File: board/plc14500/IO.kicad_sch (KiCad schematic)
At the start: 72 parts, among them U1 74HC14, U2 4051, U3 74HC14, U5 4099

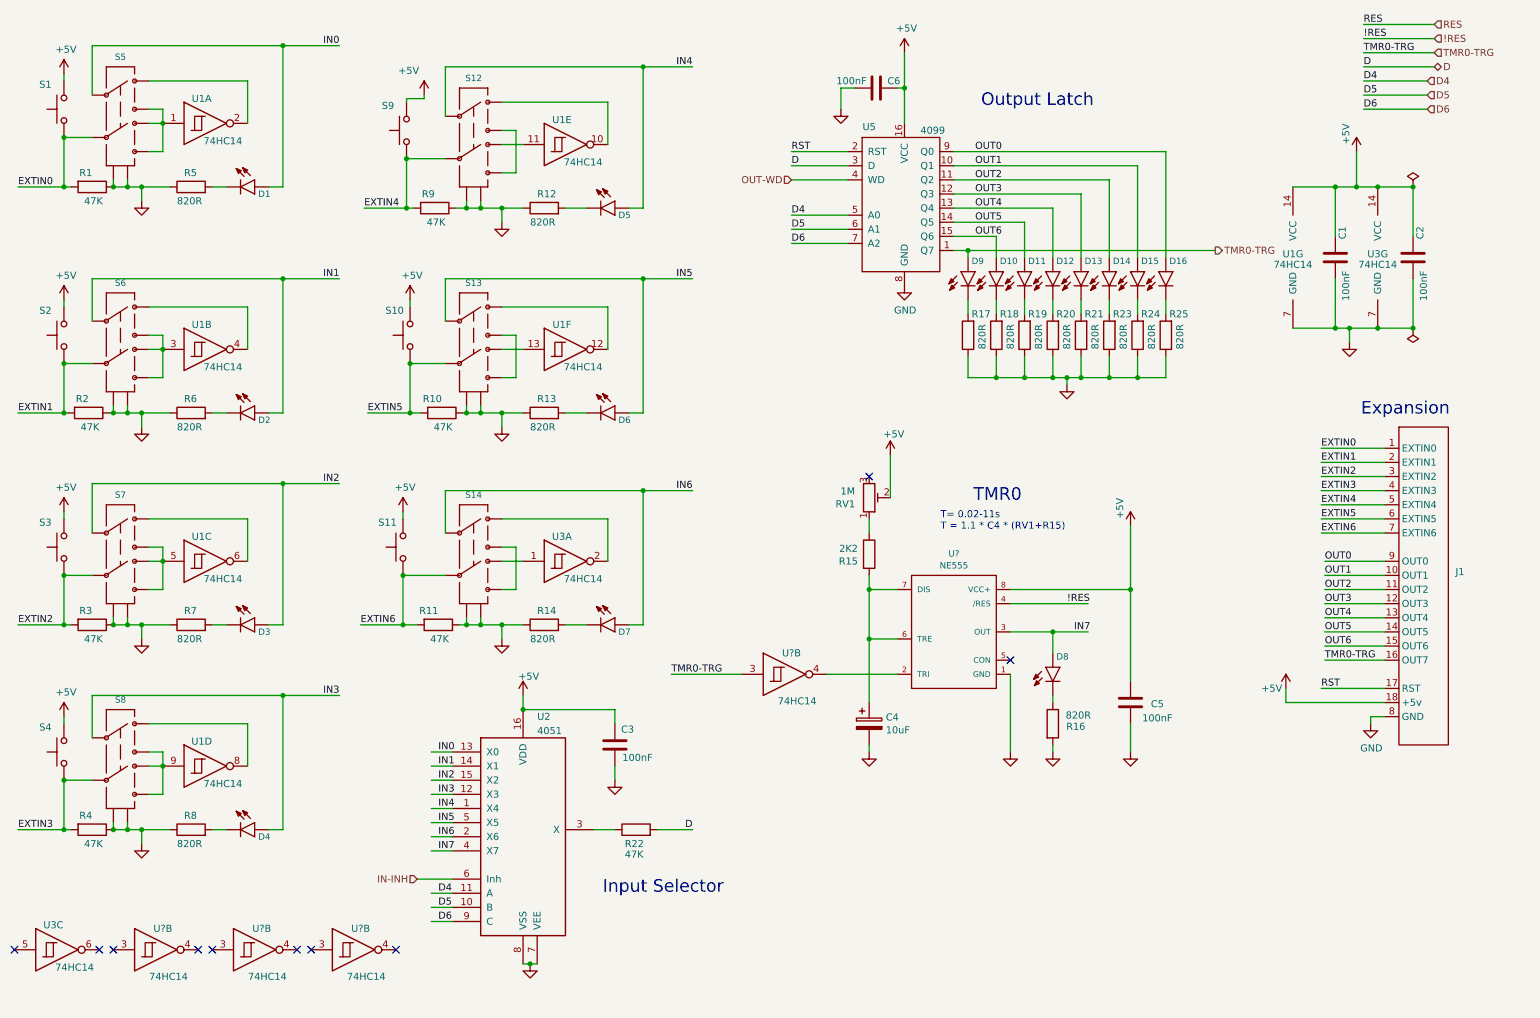
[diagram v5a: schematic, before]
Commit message: Fix issues on REV.D0
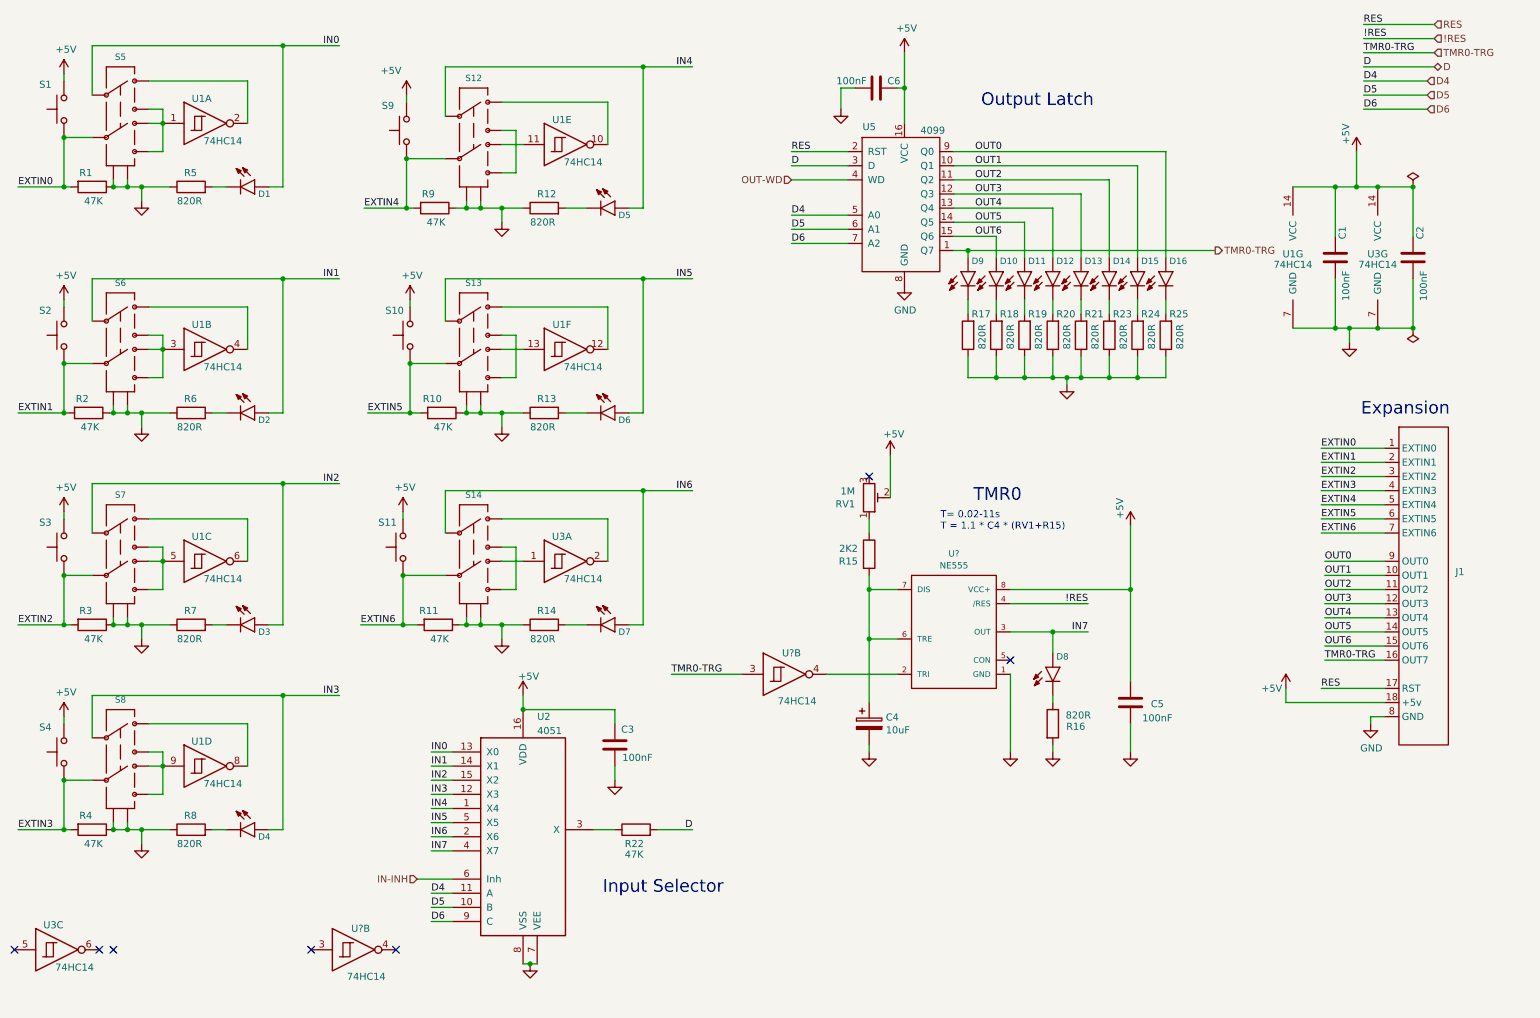
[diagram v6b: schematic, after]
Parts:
- removed U? (x2): 74HC14, Package_DIP:DIP-14_W7.62mm_LongPads, symbol plc14500:74HC14
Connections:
- net RST is gone; now on net RES: J1.17 (RST), U5.2 (RST)
- no-connect marks 10 -> 7
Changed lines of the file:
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@@
   (junction (at 105.41 142.24) (diameter 0) (color 0 0 0 0)
   )
-  (no_connect (at 46.99 185.42))
   (no_connect (at 29.21 185.42))
-  (no_connect (at 64.77 185.42))
-  (no_connect (at 49.53 185.42))
   (no_connect (at 67.31 185.42))
   (no_connect (at 167.64 100.33))
@@
     (stroke (width 0) (type default))
   )
-  (wire (pts (xy 84.455 32.385) (xy 84.455 33.02))
+  (wire (pts (xy 84.455 31.75) (xy 84.455 33.02))
     (stroke (width 0) (type default))
   )
@@
     (stroke (width 0) (type default))
   )
-  (wire (pts (xy 87.63 32.385) (xy 87.63 31.75))
-    (stroke (width 0) (type default))
-  )
   (wire (pts (xy 36.83 91.44) (xy 36.83 88.9))
     (stroke (width 0) (type default))
@@
     (stroke (width 0) (type default))
   )
-  (wire (pts (xy 84.455 32.385) (xy 87.63 32.385))
-    (stroke (width 0) (type default))
-  )
   (wire (pts (xy 172.72 30.48) (xy 173.99 30.48))
     (stroke (width 0) (type default))
@@
     (effects (font (size 2.2606 2.2606)) (justify right bottom))
   )
-  (label "IN0" (at 90.17 149.86 0) (fields_autoplaced)
+  (label "IN0" (at 88.9 149.86 0) (fields_autoplaced)
     (effects (font (size 1.27 1.27)) (justify left bottom))
   )
@@
     (effects (font (size 1.27 1.27)) (justify left bottom))
   )
-  (label "IN2" (at 90.17 154.94 0) (fields_autoplaced)
+  (label "IN2" (at 88.9 154.94 0) (fields_autoplaced)
     (effects (font (size 1.27 1.27)) (justify left bottom))
   )
@@
     (effects (font (size 1.27 1.27)) (justify left bottom))
   )
-  (label "D4" (at 90.17 175.26 0) (fields_autoplaced)
+  (label "D4" (at 88.9 175.26 0) (fields_autoplaced)
     (effects (font (size 1.27 1.27)) (justify left bottom))
   )
-  (label "RST" (at 153.67 41.91 0) (fields_autoplaced)
+  (label "RES" (at 153.67 41.91 0) (fields_autoplaced)
     (effects (font (size 1.27 1.27)) (justify left bottom))
   )
@@
     (effects (font (size 1.27 1.27)) (justify right bottom))
   )
-  (label "IN7" (at 204.47 128.27 0) (fields_autoplaced)
-    (effects (font (size 1.27 1.27)) (justify left bottom))
+  (label "IN7" (at 207.01 128.27 180) (fields_autoplaced)
+    (effects (font (size 1.27 1.27)) (justify right bottom))
   )
   (label "D4" (at 153.67 53.34 0) (fields_autoplaced)
@@
     (effects (font (size 1.27 1.27)) (justify right bottom))
   )
-  (label "!RES" (at 203.2 123.19 0) (fields_autoplaced)
-    (effects (font (size 1.27 1.27)) (justify left bottom))
+  (label "!RES" (at 207.01 123.19 180) (fields_autoplaced)
+    (effects (font (size 1.27 1.27)) (justify right bottom))
   )
-  (label "IN1" (at 90.17 152.4 0) (fields_autoplaced)
+  (label "IN1" (at 88.9 152.4 0) (fields_autoplaced)
     (effects (font (size 1.27 1.27)) (justify left bottom))
   )
@@
     (effects (font (size 1.27 1.27)) (justify left bottom))
   )
-  (label "IN5" (at 90.17 162.56 0) (fields_autoplaced)
+  (label "IN5" (at 88.9 162.56 0) (fields_autoplaced)
     (effects (font (size 1.27 1.27)) (justify left bottom))
   )
@@
     (effects (font (size 1.27 1.27)) (justify left bottom))
   )
-  (label "D6" (at 90.17 180.34 0) (fields_autoplaced)
+  (label "D6" (at 88.9 180.34 0) (fields_autoplaced)
     (effects (font (size 1.27 1.27)) (justify left bottom))
   )
@@
     (effects (font (size 1.27 1.27)) (justify left bottom))
   )
-  (label "IN7" (at 90.17 167.64 0) (fields_autoplaced)
+  (label "IN7" (at 88.9 167.64 0) (fields_autoplaced)
     (effects (font (size 1.27 1.27)) (justify left bottom))
   )
@@
     (effects (font (size 1.27 1.27)) (justify left bottom))
   )
-  (label "RST" (at 248.92 138.43 0) (fields_autoplaced)
+  (label "RES" (at 248.92 138.43 0) (fields_autoplaced)
     (effects (font (size 1.27 1.27)) (justify left bottom))
   )
@@
     (effects (font (size 1.27 1.27)) (justify left bottom))
   )
-  (label "IN4" (at 90.17 160.02 0) (fields_autoplaced)
+  (label "IN4" (at 88.9 160.02 0) (fields_autoplaced)
     (effects (font (size 1.27 1.27)) (justify left bottom))
   )
@@
     (effects (font (size 1.27 1.27)) (justify right bottom))
   )
-  (label "D5" (at 90.17 177.8 0) (fields_autoplaced)
+  (label "D5" (at 88.9 177.8 0) (fields_autoplaced)
     (effects (font (size 1.27 1.27)) (justify left bottom))
   )
@@
     (effects (font (size 1.27 1.27)) (justify left bottom))
   )
-  (label "IN6" (at 90.17 165.1 0) (fields_autoplaced)
+  (label "IN6" (at 88.9 165.1 0) (fields_autoplaced)
     (effects (font (size 1.27 1.27)) (justify left bottom))
   )
@@
     (effects (font (size 1.27 1.27)) (justify left bottom))
   )
-  (label "IN3" (at 90.17 157.48 0) (fields_autoplaced)
+  (label "IN3" (at 88.9 157.48 0) (fields_autoplaced)
     (effects (font (size 1.27 1.27)) (justify left bottom))
   )
@@
     )
   )
-  (symbol (lib_id "power:+5V") (at 87.63 31.75 0) (unit 1)
+  (symbol (lib_id "power:+5V") (at 84.455 31.75 0) (unit 1)
     (in_bom yes) (on_board yes) (dnp no)
-    (property "Reference" "#PWR015" (at 87.63 35.56 0)
+    (property "Reference" "#PWR015" (at 84.455 35.56 0)
       (effects (font (size 1.27 1.27)) hide)
     )
-    (property "Value" "+5V" (at 84.836 27.3558 0)
+    (property "Value" "+5V" (at 81.661 27.3558 0)
       (effects (font (size 1.27 1.27)))
     )
-    (property "Footprint" "" (at 87.63 31.75 0)
+    (property "Footprint" "" (at 84.455 31.75 0)
       (effects (font (size 1.27 1.27)) hide)
     )
-    (property "Datasheet" "" (at 87.63 31.75 0)
+    (property "Datasheet" "" (at 84.455 31.75 0)
       (effects (font (size 1.27 1.27)) hide)
     )
@@
     )
   )
-  (symbol (lib_id "plc14500:74HC14") (at 39.37 185.42 0) (unit 2)
-    (in_bom yes) (on_board yes) (dnp no)
-    (property "Reference" "U?" (at 40.64 181.61 0)
-      (effects (font (size 1.27 1.27)))
-    )
-    (property "Value" "74HC14" (at 41.656 190.246 0)
-      (effects (font (size 1.27 1.27)))
-    )
-    (property "Footprint" "Package_DIP:DIP-14_W7.62mm_LongPads" (at 39.37 185.42 0)
-      (effects (font (size 1.27 1.27)) hide)
-    )
-    (property "Datasheet" "http://www.ti.com/lit/gpn/sn74HC14" (at 39.37 185.42 0)
-      (effects (font (size 1.27 1.27)) hide)
-    )
-    (property "Price" "0.16" (at 39.37 185.42 0)
-      (effects (font (size 1.27 1.27)) hide)
-    )
-    (pin "1")
-    (pin "2")
-    (pin "3")
-    (pin "4")
-    (pin "5")
-    (pin "6")
-    (pin "8")
-    (pin "9")
-    (pin "10")
-    (pin "11")
-    (pin "12")
-    (pin "13")
-    (pin "14")
-    (pin "7")
-    (instances
-      (project "plc14500"
-        (path "/e5c24396-229a-4727-a88d-8f28d7f70179/00000000-0000-0000-0000-00006394a5b3"
-          (reference "U?") (unit 2)
-        )
-        (path "/e5c24396-229a-4727-a88d-8f28d7f70179"
-          (reference "U?") (unit 1)
-        )
-        (path "/e5c24396-229a-4727-a88d-8f28d7f70179/00000000-0000-0000-0000-000063b4bda9"
-          (reference "U11") (unit 4)
-        )
-      )
-    )
-  )
   (symbol (lib_id "Device:C") (at 251.46 60.96 180) (unit 1)
     (in_bom yes) (on_board yes) (dnp no)
@@
         )
       )
-    )
-  )
-  (symbol (lib_id "plc14500:74HC14") (at 57.15 185.42 0) (unit 2)
-    (in_bom yes) (on_board yes) (dnp no)
-    (property "Reference" "U?" (at 58.42 181.61 0)
-      (effects (font (size 1.27 1.27)))
-    )
-    (property "Value" "74HC14" (at 59.436 190.246 0)
-      (effects (font (size 1.27 1.27)))
-    )
-    (property "Footprint" "Package_DIP:DIP-14_W7.62mm_LongPads" (at 57.15 185.42 0)
-      (effects (font (size 1.27 1.27)) hide)
-    )
-    (property "Datasheet" "http://www.ti.com/lit/gpn/sn74HC14" (at 57.15 185.42 0)
-      (effects (font (size 1.27 1.27)) hide)
-    )
-    (property "Price" "0.16" (at 57.15 185.42 0)
-      (effects (font (size 1.27 1.27)) hide)
-    )
-    (pin "1")
-    (pin "2")
-    (pin "3")
-    (pin "4")
-    (pin "5")
-    (pin "6")
-    (pin "8")
-    (pin "9")
-    (pin "10")
-    (pin "11")
-    (pin "12")
-    (pin "13")
-    (pin "14")
-    (pin "7")
-    (instances
-      (project "plc14500"
-        (path "/e5c24396-229a-4727-a88d-8f28d7f70179/00000000-0000-0000-0000-00006394a5b3"
-          (reference "U?") (unit 2)
-        )
-        (path "/e5c24396-229a-4727-a88d-8f28d7f70179"
-          (reference "U?") (unit 1)
-        )
-        (path "/e5c24396-229a-4727-a88d-8f28d7f70179/00000000-0000-0000-0000-000063b4bda9"
-          (reference "U11") (unit 5)
-        )
-      )
